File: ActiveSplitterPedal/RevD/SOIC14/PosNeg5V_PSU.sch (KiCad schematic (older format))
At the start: 11 parts, among them U1 SE8250X2, U14 ISA0505, U15 MCP1754S-3302xCB, U16 TC593002ECB

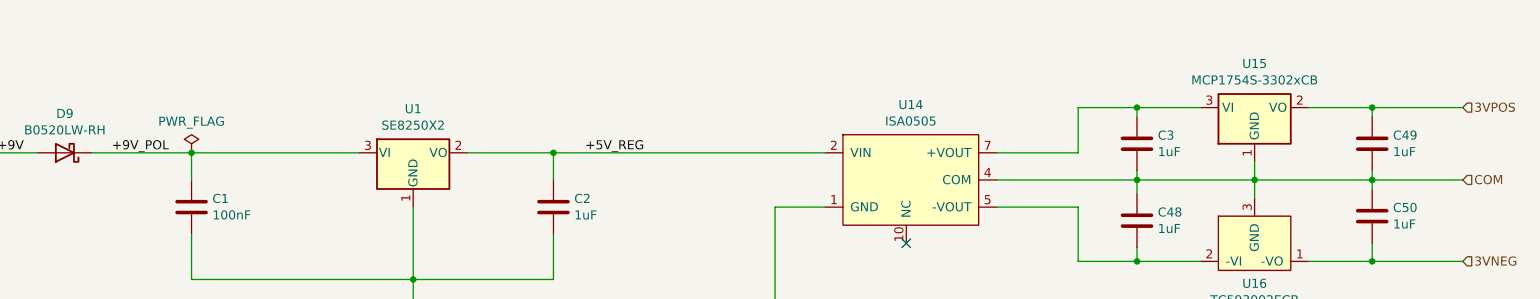
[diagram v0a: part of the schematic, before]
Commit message: updated hw
- Changed first regulator from SE8250X2 to AP7370
- Tested PSU block, added notes to schematic. No load test yet.
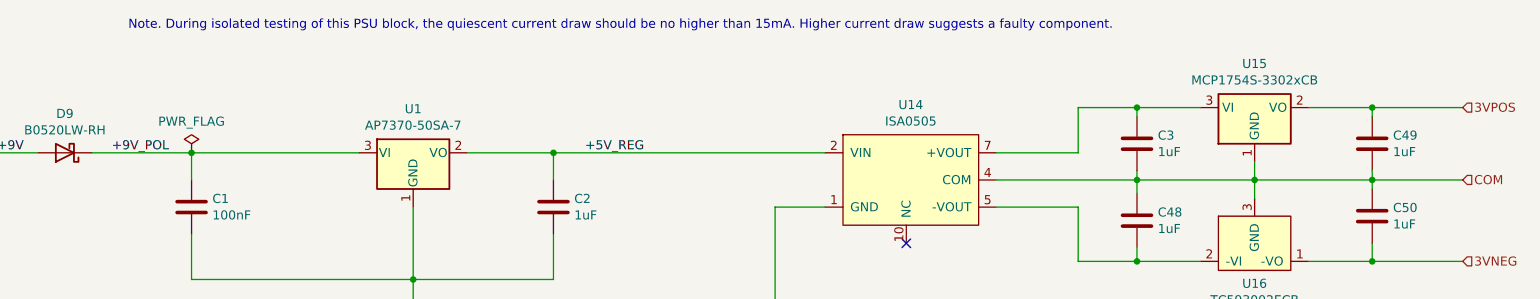
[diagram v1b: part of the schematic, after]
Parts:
- U1: value SE8250X2 -> AP7370-50SA-7
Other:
- note added: "Note. During isolated testing of this PSU block, the quiescent current draw should be no higher than 15mA. Higher current draw suggests a faulty component."
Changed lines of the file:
@@
 P 3600 2450
 F 0 "U1" H 3600 2692 50  0000 C CNN
-F 1 "SE8250X2" H 3600 2601 50  0000 C CNN
+F 1 "AP7370-50SA-7" H 3600 2601 50  0000 C CNN
 F 2 "Package_TO_SOT_SMD:SOT-23" H 3600 2675 50  0001 C CNN
-F 3 "https://datasheet.lcsc.com/szlcsc/1910181014_Seaward-Elec-SE8250X2_C437589.pdf" H 3600 2450 50  0001 C CNN
+F 3 "https://www.diodes.com/assets/Datasheets/AP7370.pdf" H 3600 2450 50  0001 C CNN
 	1    3600 2450
 	1    0    0    -1
 $EndComp
+Text Notes 2025 1775 0    50   ~ 0
+Note. During isolated testing of this PSU block, the quiescent current draw should be no higher than 15mA. Higher current draw suggests a faulty component.
 $EndSCHEMATC

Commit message: Completed RevD
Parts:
- added TP1, TP2, TP3: TestPoint, TestPoint:TestPoint_Pad_1.0x1.0mm, symbol Connector:TestPoint
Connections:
- net 3VNEG: now also TP3.1
- net 3VPOS: now also TP1.1
- net COM: now also TP2.1
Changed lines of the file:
@@
 Connection ~ 8900 2200
-Wire Wire Line
-	8900 2200 9400 2200
 Wire Wire Line
 	8900 2950 8900 3050
@@
 Text Notes 2025 1775 0    50   ~ 0
 Note. During isolated testing of this PSU block, the quiescent current draw should be no higher than 15mA. Higher current draw suggests a faulty component.
+Wire Wire Line
+	8900 2200 9400 2200
+$Comp
+L Connector:TestPoint TP1
+U 1 1 5F5F191B
+P 8050 5775
+F 0 "TP1" H 8108 5893 50  0000 L CNN
+F 1 "TestPoint" H 8108 5802 50  0000 L CNN
+F 2 "TestPoint:TestPoint_Pad_1.0x1.0mm" H 8250 5775 50  0001 C CNN
+F 3 "~" H 8250 5775 50  0001 C CNN
+	1    8050 5775
+	1    0    0    -1
+$EndComp
+Wire Wire Line
+	8050 5775 8050 5900
+$Comp
+L Connector:TestPoint TP2
+U 1 1 5F5F21CE
+P 8675 5775
+F 0 "TP2" H 8733 5893 50  0000 L CNN
+F 1 "TestPoint" H 8733 5802 50  0000 L CNN
+F 2 "TestPoint:TestPoint_Pad_1.0x1.0mm" H 8875 5775 50  0001 C CNN
+F 3 "~" H 8875 5775 50  0001 C CNN
+	1    8675 5775
+	1    0    0    -1
+$EndComp
+Wire Wire Line
+	8675 5775 8675 5900
+$Comp
+L Connector:TestPoint TP3
+U 1 1 5F5F2A34
+P 9300 5775
+F 0 "TP3" H 9358 5893 50  0000 L CNN
+F 1 "TestPoint" H 9358 5802 50  0000 L CNN
+F 2 "TestPoint:TestPoint_Pad_1.0x1.0mm" H 9500 5775 50  0001 C CNN
+F 3 "~" H 9500 5775 50  0001 C CNN
+	1    9300 5775
+	1    0    0    -1
+$EndComp
+Wire Wire Line
+	9300 5775 9300 5900
+Text HLabel 9300 5900 3    50   Input ~ 0
+3VNEG
+Text HLabel 8675 5900 3    50   Input ~ 0
+COM
+Text HLabel 8050 5900 3    50   Input ~ 0
+3VPOS
 $EndSCHEMATC
